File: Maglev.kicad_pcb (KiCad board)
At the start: 4 copper layers, 265 x 130 mm, 129 parts, among them IC1 TLV1117LV33DCYR, J1 USB_C_Receptacle, J11 690367190672, J12 690367190672, J2 691103110002, J3 61300621121, J4 61300821121, J6 61300621121, J7 690367191672, J8 690367191672, U1 WE-TVS-82400102, U2 ESP32-C3, U4 TMAG5173A2QDBVRQ1, U5 TPS259474ARPWR, Y1 IQXC-42_830108213209

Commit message: cleared some rule checker errors
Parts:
- removed HALL: ~, CUSTOM:MagnetRing
- J1: value USB_C_Receptacle -> 629722000214
- MB?: renamed from REF**1; value BreakLine_1h_D0.5mm_P0.85mm -> (none); footprint Panelization:BreakLine_1h_D0.5mm_P0.85mm -> CUSTOM:BreakLine_1h_D0.5mm_P0.85mm
- MB?: renamed from REF**3; value BreakLine_1h_D0.5mm_P0.85mm -> (none); footprint Panelization:BreakLine_1h_D0.5mm_P0.85mm -> CUSTOM:BreakLine_1h_D0.5mm_P0.85mm
- MB?: renamed from REF**7; value BreakLine_1h_D0.5mm_P0.85mm -> (none); footprint Panelization:BreakLine_1h_D0.5mm_P0.85mm -> CUSTOM:BreakLine_1h_D0.5mm_P0.85mm
- MB?: renamed from REF**11; value BreakLine_1h_D0.5mm_P0.85mm -> (none); footprint Panelization:BreakLine_1h_D0.5mm_P0.85mm -> CUSTOM:BreakLine_1h_D0.5mm_P0.85mm
- MB?: renamed from REF**12; value BreakLine_1h_D0.5mm_P0.85mm -> (none); footprint Panelization:BreakLine_1h_D0.5mm_P0.85mm -> CUSTOM:BreakLine_1h_D0.5mm_P0.85mm
- MB?: renamed from ?; footprint (none) -> CUSTOM:BreakLine_1h_D0.5mm_P0.85mm
- MB?: renamed from REF**6; value BreakLine_1h_D0.5mm_P0.85mm -> (none); footprint Panelization:BreakLine_1h_D0.5mm_P0.85mm -> CUSTOM:BreakLine_1h_D0.5mm_P0.85mm
- MB?: renamed from 12; footprint (none) -> CUSTOM:BreakLine_1h_D0.5mm_P0.85mm
- MB?: renamed from REF**; value BreakLine_1h_D0.5mm_P0.85mm -> (none); footprint Panelization:BreakLine_1h_D0.5mm_P0.85mm -> CUSTOM:BreakLine_1h_D0.5mm_P0.85mm
- MB?: renamed from 4; footprint (none) -> CUSTOM:BreakLine_1h_D0.5mm_P0.85mm
- MB?: renamed from 6; footprint (none) -> CUSTOM:BreakLine_1h_D0.5mm_P0.85mm
- MB?: renamed from REF**9; value BreakLine_1h_D0.5mm_P0.85mm -> (none); footprint Panelization:BreakLine_1h_D0.5mm_P0.85mm -> CUSTOM:BreakLine_1h_D0.5mm_P0.85mm
- MB?: renamed from 7; footprint (none) -> CUSTOM:BreakLine_1h_D0.5mm_P0.85mm
- MB?: renamed from 11; footprint (none) -> CUSTOM:BreakLine_1h_D0.5mm_P0.85mm
- MB?: renamed from 3; footprint (none) -> CUSTOM:BreakLine_1h_D0.5mm_P0.85mm
- MB?: renamed from 9; footprint (none) -> CUSTOM:BreakLine_1h_D0.5mm_P0.85mm
- MB?: renamed from REF**4; value BreakLine_1h_D0.5mm_P0.85mm -> (none); footprint Panelization:BreakLine_1h_D0.5mm_P0.85mm -> CUSTOM:BreakLine_1h_D0.5mm_P0.85mm
- MB?: renamed from 1; footprint (none) -> CUSTOM:BreakLine_1h_D0.5mm_P0.85mm
- U1: footprint SOT95P280X116-6N:SOT95P280X116-6N -> Package_TO_SOT_SMD:SOT-23-6
- moved J1 0.08 mm to (258.4, 143.4)
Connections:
- J1 pad B8: unconnected-(J1-SBU2-PadB8) -> unconnected-(J1-SBU1-PadA8)
- J1 pad S2: (no net) -> GND
- J1 pad S3: (no net) -> GND
- J1 pad S4: (no net) -> GND

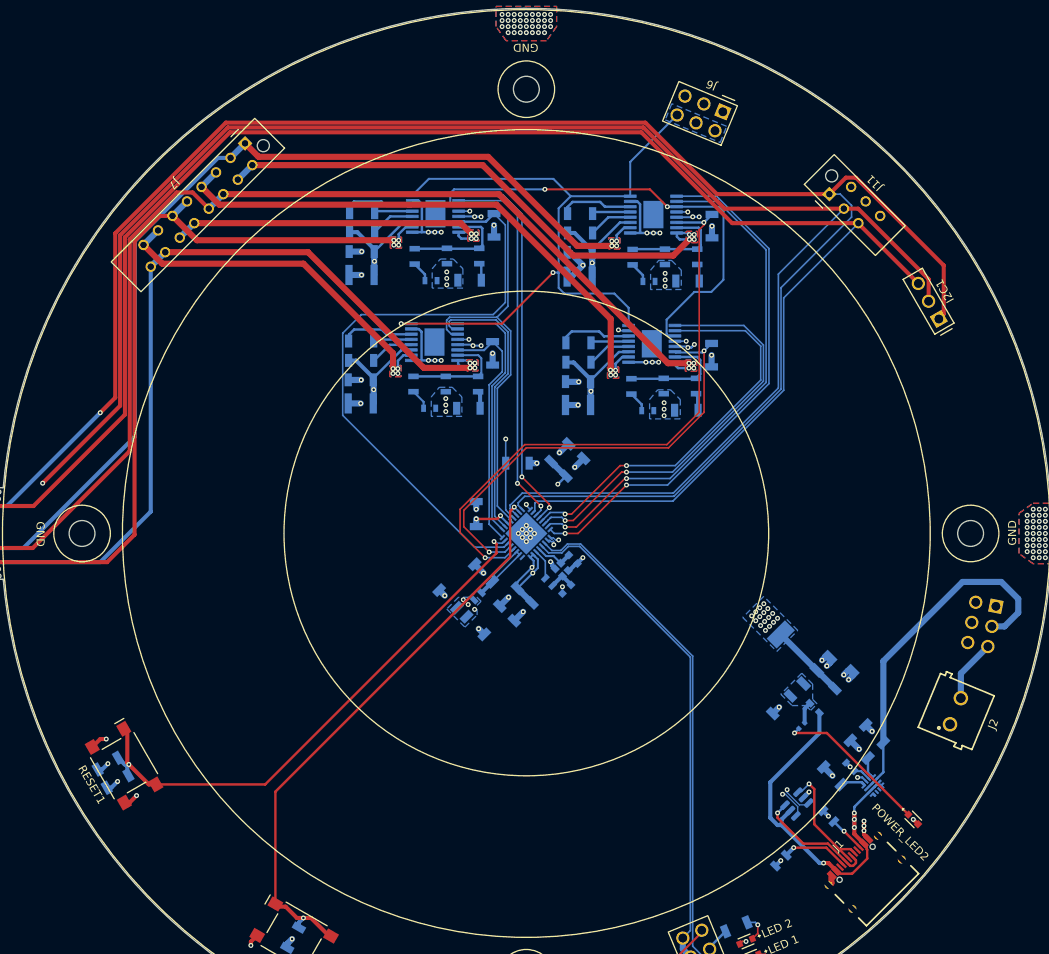
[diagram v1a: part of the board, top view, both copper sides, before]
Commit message: testpoints added
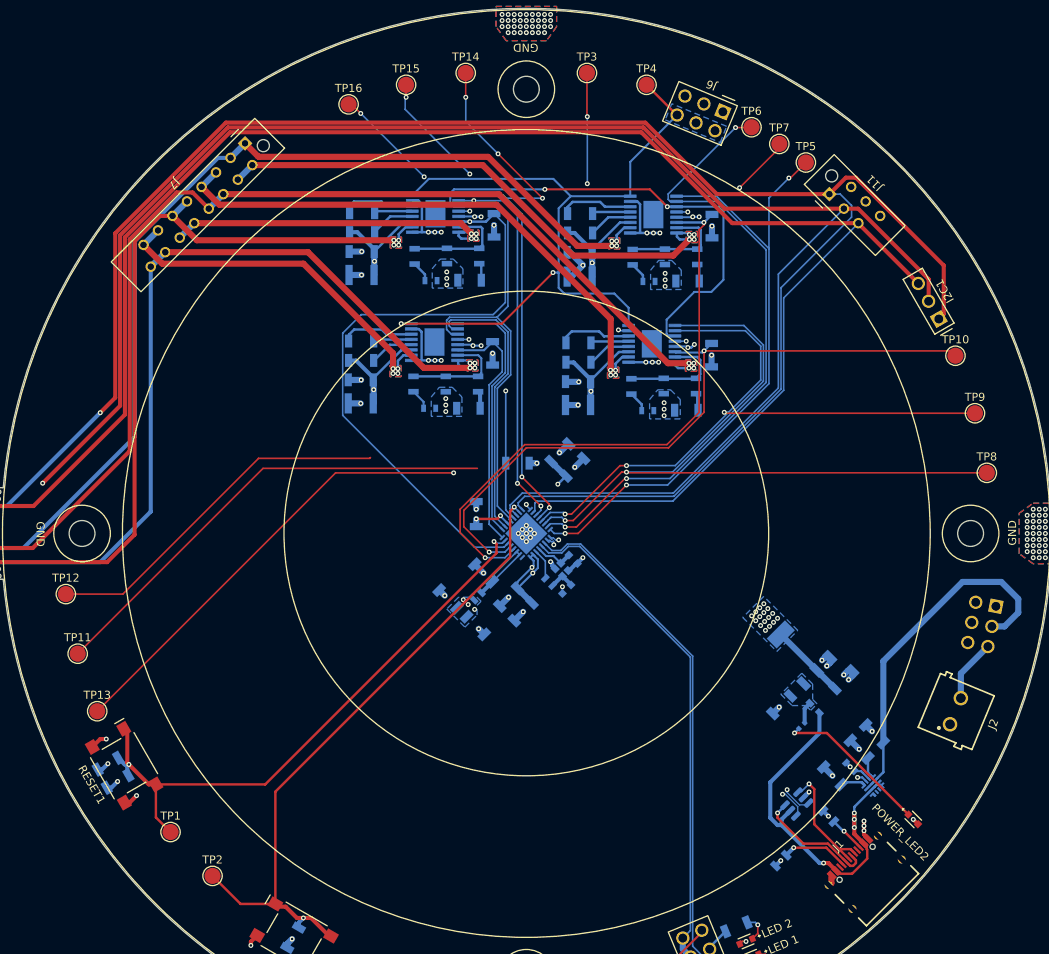
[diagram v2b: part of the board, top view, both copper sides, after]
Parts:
- added TP1: TP:CHIP_EN, TestPoint:TestPoint_Pad_D2.0mm, F.Cu at (171.0, 137.0)
- added TP10: TP:B_ISENSE, TestPoint:TestPoint_Pad_D2.0mm, F.Cu at (268.1, 78.0)
- added TP11: TP:D_PWM, TestPoint:TestPoint_Pad_D2.0mm, F.Cu at (159.5, 114.9)
- added TP12: TP:D_DIR, TestPoint:TestPoint_Pad_D2.0mm, F.Cu at (158.0, 107.5)
- added TP13: TP:D_ISENSE, TestPoint:TestPoint_Pad_D2.0mm, F.Cu at (161.9, 122.0)
- added TP14: TP:C_PWM, TestPoint:TestPoint_Pad_D2.0mm, F.Cu at (207.5, 43.0)
- added TP15: TP:C_DIR, TestPoint:TestPoint_Pad_D2.0mm, F.Cu at (200.1, 44.5)
- added TP16: TP:C_ISENSE, TestPoint:TestPoint_Pad_D2.0mm, F.Cu at (193.0, 46.9)
- added TP2: TP:BOOT, TestPoint:TestPoint_Pad_D2.0mm, F.Cu at (176.2, 142.4)
- added TP3: TP:FAULT, TestPoint:TestPoint_Pad_D2.0mm, F.Cu at (222.5, 43.0)
- added TP4: TP:PMODE, TestPoint:TestPoint_Pad_D2.0mm, F.Cu at (229.9, 44.5)
- added TP5: TP:A_PWM, TestPoint:TestPoint_Pad_D2.0mm, F.Cu at (249.6, 54.1)
- added TP6: TP:A_DIR, TestPoint:TestPoint_Pad_D2.0mm, F.Cu at (242.9, 49.7)
- added TP7: TP:A_ISENSE, TestPoint:TestPoint_Pad_D2.0mm, F.Cu at (246.3, 51.8)
- added TP8: TP:B_PWM, TestPoint:TestPoint_Pad_D2.0mm, F.Cu at (272.0, 92.5)
- added TP9: TP:B_DIR, TestPoint:TestPoint_Pad_D2.0mm, F.Cu at (270.5, 85.1)
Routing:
- net /HBRIDGE_D_PWM: track 31.9 -> 90.9 mm
- net /HBRIDGE_D_ISENSE: track 30.9 -> 87.2 mm, vias 0 -> 1
- net /HBRIDGE_D_DIR: track 35.0 -> 79.8 mm
- net /HBRIDGE_B_PWM: track 51.2 -> 95.8 mm
- net /HBRIDGE_B_DIR: track 50.1 -> 81.7 mm, vias 2 -> 3
- net /HBRIDGE_B_ISENSE: track 56.9 -> 88.3 mm
- net /HBRIDGE_C_PWM: track 48.4 -> 72.8 mm, vias 2 -> 5
- net /HBRIDGE_C_ISENSE: track 75.7 -> 96.7 mm, vias 0 -> 3
- net /HBRIDGE_C_DIR: track 46.7 -> 64.6 mm, vias 2 -> 5
- net /HBRIDG_ALL_FAULT: track 99.0 -> 116.2 mm, vias 5 -> 7
- net /HBRIDGE_A_DIR: track 65.1 -> 80.6 mm, vias 2 -> 3
- net /HBRIDGE_A_ISENSE: track 74.5 -> 88.2 mm, vias 2 -> 3
- net /HBRIDGE_A_PWM: track 65.8 -> 78.4 mm, vias 2 -> 3
- net /BOOT: track 72.2 -> 81.5 mm
- net /CHIP_EN: track 69.4 -> 76.0 mm
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
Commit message: Finished Testpoints, cleared all errors and warnings, changed copper thickness from 35um to 70um
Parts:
- added U3: ~, CUSTOM:MagnetRing, B.Cu at (80.0, 100.0)
- J1: footprint WURTH_USB:629722000214 -> WURTH_USB:629722000214_CUSTOM
- moved POWER_LED2 4.94 mm to (263.7, 140.3)
- moved TP5 3.65 mm to (250.9, 50.6)
- moved TP7 3.54 mm to (247.8, 48.6)
- moved TP2 3.50 mm to (173.8, 145.0)
- moved TP6 3.50 mm to (244.6, 46.6)
- moved TP12 3.50 mm to (154.5, 108.0)
- moved TP14 3.50 mm to (207.0, 39.5)
- moved TP3 3.50 mm to (223.0, 39.5)
- moved TP8 3.50 mm to (275.5, 92.0)
- moved TP1 3.50 mm to (168.3, 139.2)
- moved TP15 3.50 mm to (199.2, 41.1)
- moved TP4 3.50 mm to (230.8, 41.1)
- moved TP9 3.50 mm to (273.9, 84.2)
- moved TP11 3.50 mm to (156.1, 115.8)
- moved TP10 3.50 mm to (271.4, 76.7)
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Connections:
- J1 pad B8: unconnected-(J1-SBU1-PadA8) -> unconnected-(J1-SBU2-PadB8)
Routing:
- net /HBRIDGE_D_DIR: track 79.8 -> 104.6 mm, vias 0 -> 1
- net /HBRIDGE_D_ISENSE: track 87.2 -> 95.4 mm
- net /HBRIDGE_D_PWM: track 90.9 -> 96.5 mm, vias 0 -> 1
- net /HBRIDGE_B_DIR: track 81.7 -> 85.7 mm
- net /HBRIDGE_A_PWM: track 78.4 -> 82.3 mm
- net /HBRIDGE_A_ISENSE: track 88.2 -> 91.9 mm
- net /HBRIDGE_C_DIR: track 64.6 -> 68.3 mm
- net /HBRIDGE_C_PWM: track 72.8 -> 76.5 mm
- net /HBRIDGE_B_PWM: track 95.8 -> 99.4 mm
- net /HBRIDGE_C_ISENSE: track 96.7 -> 100.3 mm
- net /HBRIDG_ALL_FAULT: track 116.2 -> 119.6 mm
- net /HBRIDGE_B_ISENSE: track 88.3 -> 91.6 mm
- net /HBRIDGE_A_DIR: track 80.6 -> 83.8 mm
- net /Electromagnet Driver/PMODE: track 93.7 -> 96.7 mm
- net Net-(POWER_LED2-+): track 19.1 -> 21.9 mm
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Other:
- board text added: "Felix Baechle 310312 Luca Denz xxXXxx Projectwork HTWG SS2026 assisted by H. Rebholz"

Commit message: cleared some ERC errors/warnings in schematic, still one main error category to be solved
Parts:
- EMA1, EMB1, EMC1, EMD1: footprint SOP65P640X120-17N:SOP65P640X120-17N -> DRV8874PWPR:SOP65P640X120-17N
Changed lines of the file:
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@@
 		(capping no)
 		(filling no)
-		(zone_defaults)
 		(grid_origin 215 100)
 		(pcbplotparams
@@
 			(unit
 				(name "A")
-				(pins "1" "3" "2" "4")
+				(pins "1" "2" "3" "4")
 			)
 		)
@@
 			(unit
 				(name "A")
-				(pins "1" "3" "2" "4")
+				(pins "1" "2" "3" "4")
 			)
 		)
@@
 		)
 	)
-	(footprint "SOP65P640X120-17N:SOP65P640X120-17N"
+	(footprint "DRV8874PWPR:SOP65P640X120-17N"
 		(layer "B.Cu")
 		(at 203.628066 76.302233 180)
@@
 				(font
 					(size 1.27 1.27)
-					(thickness 0.15)
 				)
 				(justify mirror)
@@
 				(font
 					(size 1.27 1.27)
-					(thickness 0.15)
 				)
 				(justify mirror)
@@
 		)
 		(property "MF" "Texas Instruments"
-			(at 0 0 0)
+			(at 0 0 180)
 			(unlocked yes)
 			(layer "B.Fab")
@@
 		)
 		(property "Package" "HTSSOP-16 Texas Instruments"
-			(at 0 0 0)
+			(at 0 0 180)
 			(unlocked yes)
 			(layer "B.Fab")
@@
 		)
 		(property "Price" "None"
-			(at 0 0 0)
+			(at 0 0 180)
 			(unlocked yes)
 			(layer "B.Fab")
@@
 		)
 		(property "SnapEDA_Link" "https://www.snapeda.com/parts/DRV8874PWPR/Texas+Instruments/view-part/?ref=snap"
-			(at 0 0 0)
+			(at 0 0 180)
 			(unlocked yes)
 			(layer "B.Fab")
@@
 		)
 		(property "MP" "DRV8874PWPR"
-			(at 0 0 0)
+			(at 0 0 180)
 			(unlocked yes)
 			(layer "B.Fab")
@@
 		)
 		(property "Availability" "In Stock"
-			(at 0 0 0)
+			(at 0 0 180)
 			(unlocked yes)
 			(layer "B.Fab")
@@
 		)
 		(property "Check_prices" "https://www.snapeda.com/parts/DRV8874PWPR/Texas+Instruments/view-part/?ref=eda"
-			(at 0 0 0)
+			(at 0 0 180)
 			(unlocked yes)
 			(layer "B.Fab")
@@
 			(unit
 				(name "A")
-				(pins "3" "1" "2" "4")
+				(pins "1" "2" "3" "4")
 			)
 		)
@@
 			(net "+3.3V")
 			(pinfunction "OUTPUT_2_4")
-			(pintype "passive")
+			(pintype "output")
 		)
 		(embedded_fonts no)
@@
 			(net "/HBRIDGE_A_ISENSE")
 			(pinfunction "XTAL_32K_P/ADC1_CH0_4")
-			(pintype "output")
+			(pintype "input")
 		)
 		(pad "5" smd roundrect
@@
 		)
 	)
-	(footprint "SOP65P640X120-17N:SOP65P640X120-17N"
+	(footprint "DRV8874PWPR:SOP65P640X120-17N"
 		(layer "B.Cu")
 		(at 203.749466 60.425 180)
@@
 				(font
 					(size 1.27 1.27)
-					(thickness 0.15)
 				)
 				(justify mirror)
@@
 				(font
 					(size 1.27 1.27)
-					(thickness 0.15)
 				)
 				(justify mirror)
@@
 		)
 		(property "MF" "Texas Instruments"
-			(at 0 0 0)
+			(at 0 0 180)
 			(unlocked yes)
 			(layer "B.Fab")
@@
 		)
 		(property "Package" "HTSSOP-16 Texas Instruments"
-			(at 0 0 0)
+			(at 0 0 180)
 			(unlocked yes)
 			(layer "B.Fab")
@@
 		)
 		(property "Price" "None"
-			(at 0 0 0)
+			(at 0 0 180)
 			(unlocked yes)
 			(layer "B.Fab")
@@
 		)
 		(property "SnapEDA_Link" "https://www.snapeda.com/parts/DRV8874PWPR/Texas+Instruments/view-part/?ref=snap"
-			(at 0 0 0)
+			(at 0 0 180)
 			(unlocked yes)
 			(layer "B.Fab")
@@
 		)
 		(property "MP" "DRV8874PWPR"
-			(at 0 0 0)
+			(at 0 0 180)
 			(unlocked yes)
 			(layer "B.Fab")
@@
 		)
 		(property "Availability" "In Stock"
-			(at 0 0 0)
+			(at 0 0 180)
 			(unlocked yes)
 			(layer "B.Fab")
@@
 		)
 		(property "Check_prices" "https://www.snapeda.com/parts/DRV8874PWPR/Texas+Instruments/view-part/?ref=eda"
-			(at 0 0 0)
+			(at 0 0 180)
 			(unlocked yes)
 			(layer "B.Fab")
@@
 		)
 	)
-	(footprint "SOP65P640X120-17N:SOP65P640X120-17N"
+	(footprint "DRV8874PWPR:SOP65P640X120-17N"
 		(layer "B.Cu")
 		(at 230.531673 76.525 180)
@@
 				(font
 					(size 1.27 1.27)
-					(thickness 0.15)
 				)
 				(justify mirror)
@@
 				(font
 					(size 1.27 1.27)
-					(thickness 0.15)
 				)
 				(justify mirror)
@@
 		)
 		(property "MF" "Texas Instruments"
-			(at 0 0 0)
+			(at 0 0 180)
 			(unlocked yes)
 			(layer "B.Fab")
@@
 		)
 		(property "Package" "HTSSOP-16 Texas Instruments"
-			(at 0 0 0)
+			(at 0 0 180)
 			(unlocked yes)
 			(layer "B.Fab")
@@
 		)
 		(property "Price" "None"
-			(at 0 0 0)
+			(at 0 0 180)
 			(unlocked yes)
 			(layer "B.Fab")
@@
 		)
 		(property "SnapEDA_Link" "https://www.snapeda.com/parts/DRV8874PWPR/Texas+Instruments/view-part/?ref=snap"
-			(at 0 0 0)
+			(at 0 0 180)
 			(unlocked yes)
 			(layer "B.Fab")
@@
 		)
 		(property "MP" "DRV8874PWPR"
-			(at 0 0 0)
+			(at 0 0 180)
 			(unlocked yes)
 			(layer "B.Fab")
@@
 		)
 		(property "Availability" "In Stock"
-			(at 0 0 0)
+			(at 0 0 180)
 			(unlocked yes)
 			(layer "B.Fab")
@@
 		)
 		(property "Check_prices" "https://www.snapeda.com/parts/DRV8874PWPR/Texas+Instruments/view-part/?ref=eda"
-			(at 0 0 0)
+			(at 0 0 180)
 			(unlocked yes)
 			(layer "B.Fab")
@@
 		)
 	)
-	(footprint "SOP65P640X120-17N:SOP65P640X120-17N"
+	(footprint "DRV8874PWPR:SOP65P640X120-17N"
 		(layer "B.Cu")
 		(at 230.731673 60.525 180)
@@
 				(font
 					(size 1.27 1.27)
-					(thickness 0.15)
 				)
 				(justify mirror)
@@
 				(font
 					(size 1.27 1.27)
-					(thickness 0.15)
 				)
 				(justify mirror)
@@
 		)
 		(property "MF" "Texas Instruments"
-			(at 0 0 0)
+			(at 0 0 180)
 			(unlocked yes)
 			(layer "B.Fab")
@@
 		)
 		(property "Package" "HTSSOP-16 Texas Instruments"
-			(at 0 0 0)
+			(at 0 0 180)
 			(unlocked yes)
 			(layer "B.Fab")
@@
 		)
 		(property "Price" "None"
-			(at 0 0 0)
+			(at 0 0 180)
 			(unlocked yes)
 			(layer "B.Fab")
@@
 		)
 		(property "SnapEDA_Link" "https://www.snapeda.com/parts/DRV8874PWPR/Texas+Instruments/view-part/?ref=snap"
-			(at 0 0 0)
+			(at 0 0 180)
 			(unlocked yes)
 			(layer "B.Fab")
@@
 		)
 		(property "MP" "DRV8874PWPR"
-			(at 0 0 0)
+			(at 0 0 180)
 			(unlocked yes)
 			(layer "B.Fab")
@@
 		)
 		(property "Availability" "In Stock"
-			(at 0 0 0)
+			(at 0 0 180)
 			(unlocked yes)
 			(layer "B.Fab")
@@
 		)
 		(property "Check_prices" "https://www.snapeda.com/parts/DRV8874PWPR/Texas+Instruments/view-part/?ref=eda"
-			(at 0 0 0)
+			(at 0 0 180)
 			(unlocked yes)
 			(layer "B.Fab")
@@
 		(sheetname "/")
 		(sheetfile "Maglev.kicad_sch")
+		(units
+			(unit
+				(name "A")
+				(pins)
+			)
+		)
 		(attr smd)
 		(duplicate_pad_numbers_are_jumpers no)
@@
 	)
 	(segment
-		(start 249.453553 123.446447)
-		(end 249.453553 121.679721)
-		(width 0.508)
-		(layer "B.Cu")
-		(net "+5V")
-	)
-	(segment
-		(start 249.453553 121.679721)
-		(end 250.116637 121.016637)
-		(width 0.508)
-		(layer "B.Cu")
-		(net "+5V")
-	)
-	(segment
 		(start 210.796016 105.264644)
 		(end 213.801454 102.259206)
@@
 		(net "Net-(R35-Pad2)")
 	)
+	(segment
+		(start 249.453553 123.446447)
+		(end 249.453553 121.679721)
+		(width 0.508)
+		(layer "B.Cu")
+		(net "+5V")
+	)
+	(segment
+		(start 249.453553 121.679721)
+		(end 250.116637 121.016637)
+		(width 0.508)
+		(layer "B.Cu")
+		(net "+5V")
+	)
 	(zone
